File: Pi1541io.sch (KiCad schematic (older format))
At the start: 28 parts, among them J1 IEC1, J2 IEC2, J3 IEC3, J4 ExtSpkr, J5 GS3, J6 GS3, J7 GS3, J8 GS3, P1 Conn_02x20_Odd_Even, SW1 SW_Push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

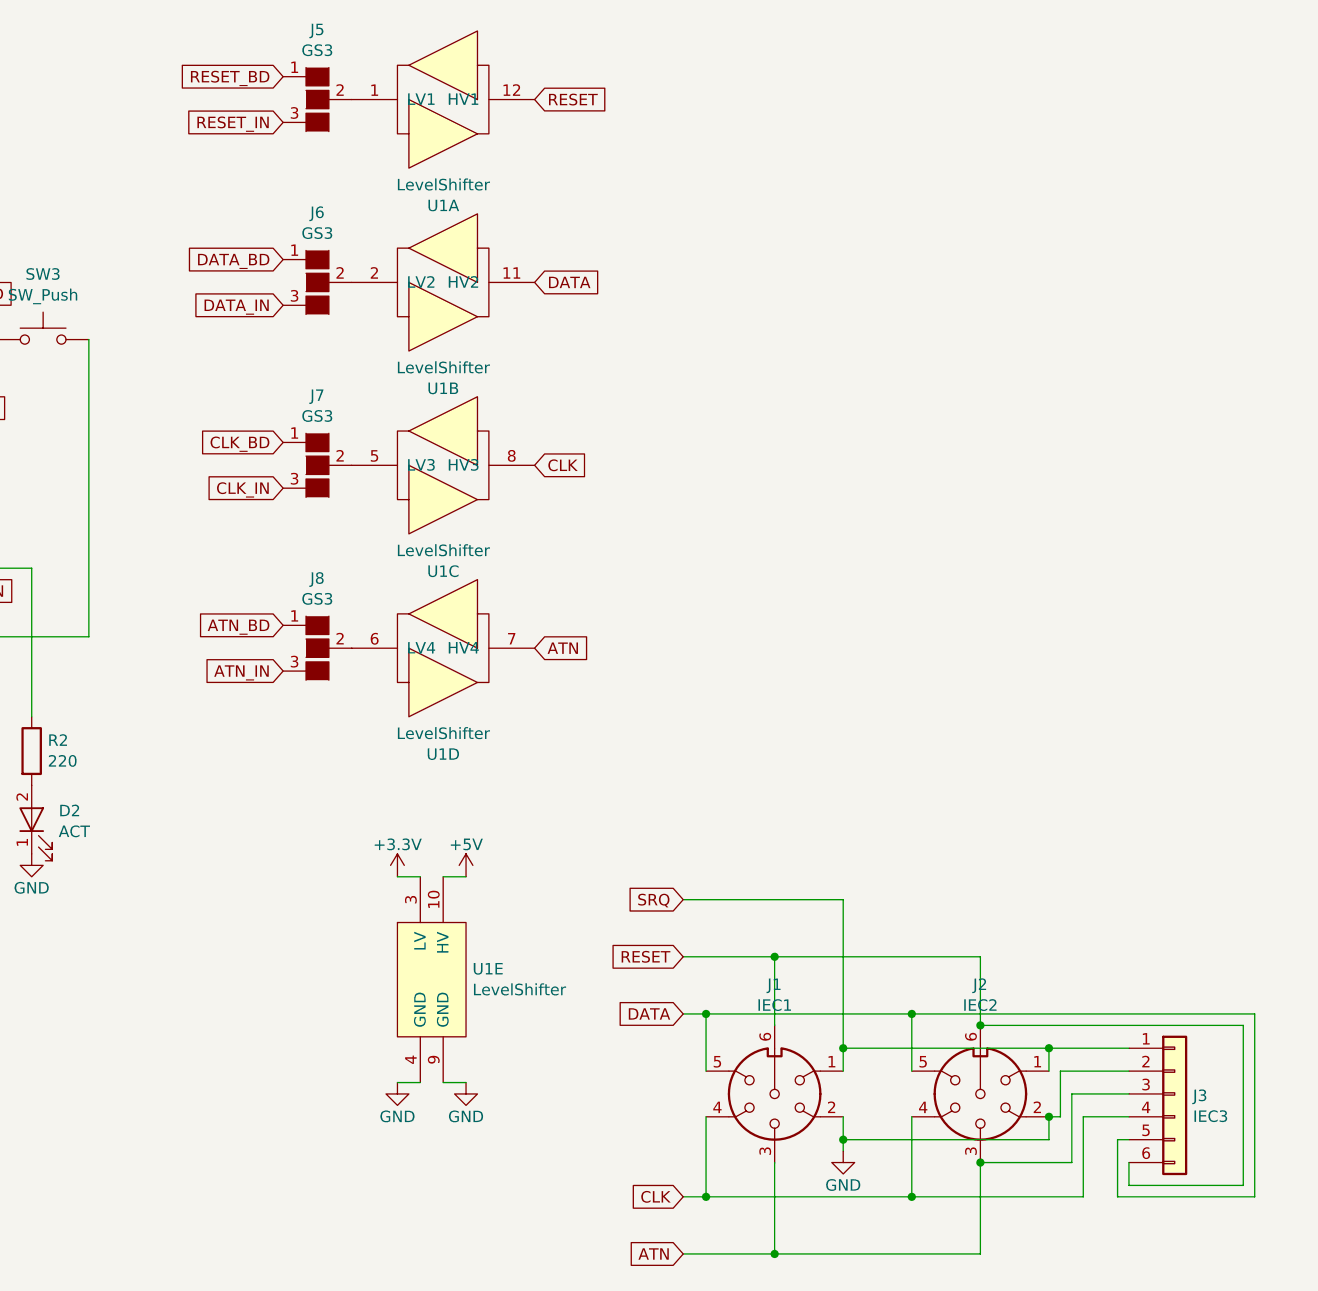
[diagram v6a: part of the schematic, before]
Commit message: Silk screen corrections. Re-added reset button.
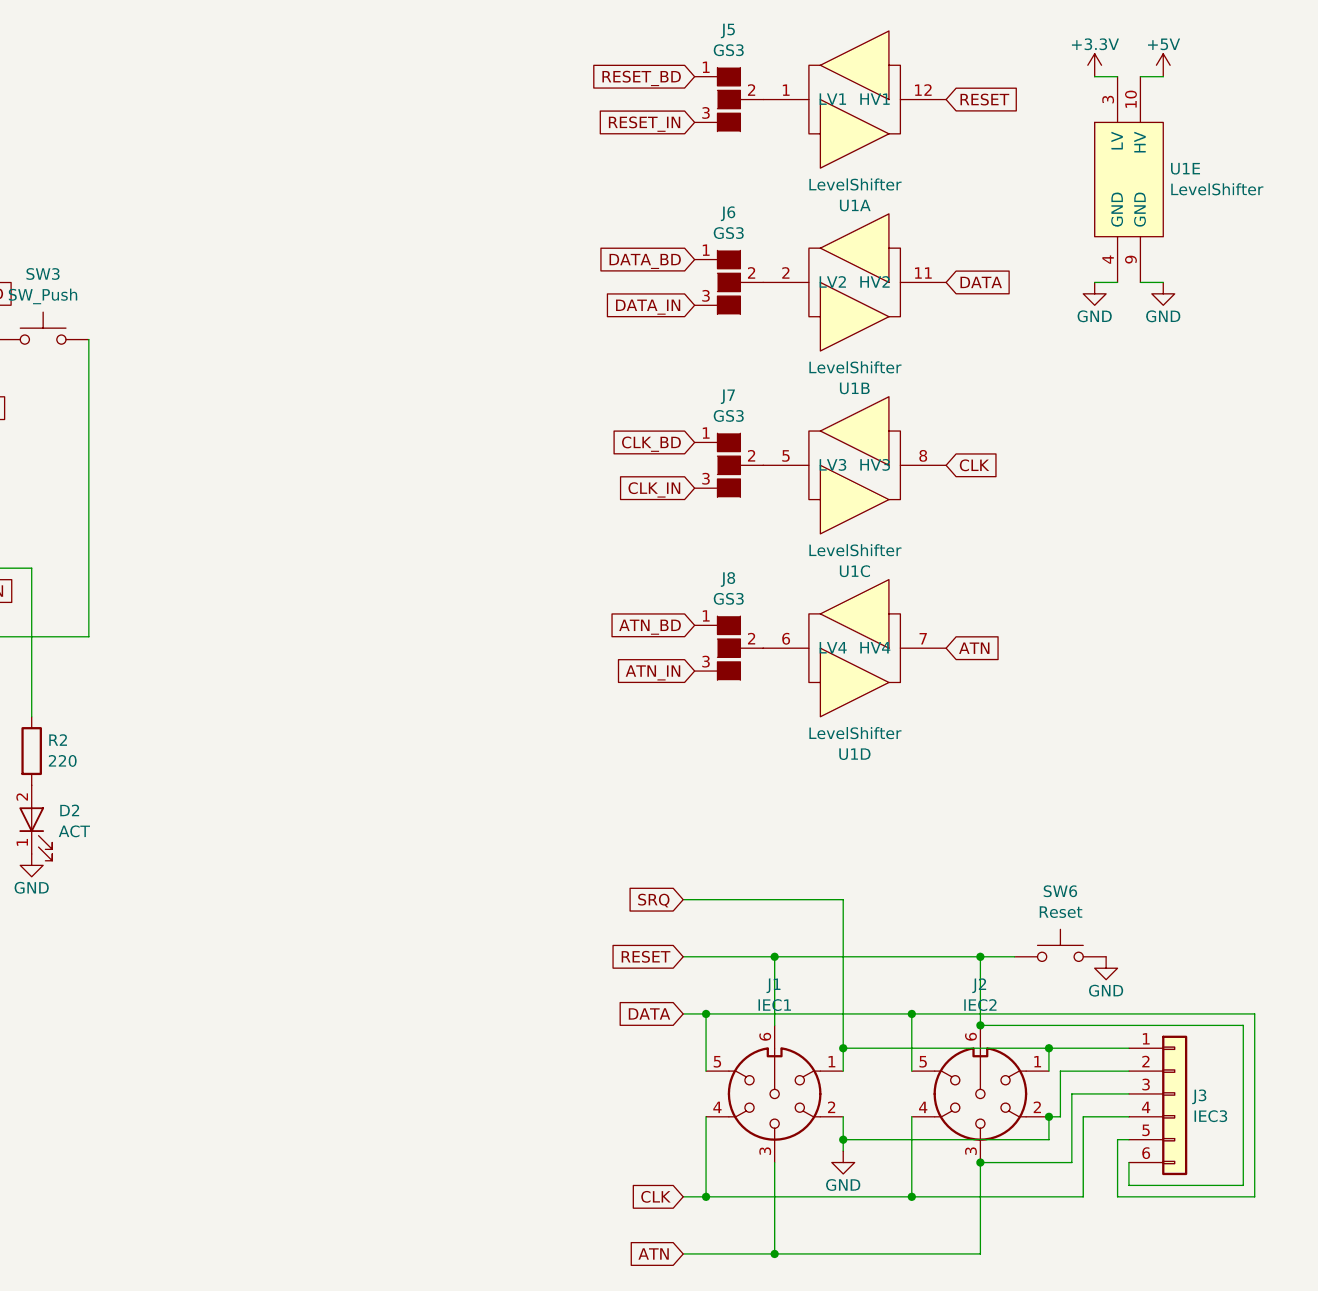
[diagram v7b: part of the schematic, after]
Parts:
- added SW6: Reset, Buttons_Switches_THT:SW_PUSH_6mm, symbol Switch:SW_Push
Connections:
- net GND: now also SW6.2
- net RESET: now also SW6.1
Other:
- moved on the sheet: J5, J6, J7, J8, U1A, U1B, U1C, U1D, U1E
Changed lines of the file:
@@
 Sheet 1 1
 Title "PI1541 IO Adapter"
-Date "2018-05-09"
-Rev "1"
+Date "2018-05-24"
+Rev "x"
 Comp "hackup.net"
 Comment1 "https://github.com/hackup/Pi1541io"
@@
 L hackup:LevelShifterModule4CH U1
 U 1 1 5AF39D90
-P 7350 1050
-F 0 "U1" H 7350 585 50  0000 C CNN
-F 1 "LevelShifter" H 7350 676 50  0000 C CNN
-F 2 "hackup:LevelShifterModule4CH" H 7350 1050 50  0001 C CNN
-F 3 "" H 7350 1050 50  0001 C CNN
-	1    7350 1050
+P 9150 1050
+F 0 "U1" H 9150 585 50  0000 C CNN
+F 1 "LevelShifter" H 9150 676 50  0000 C CNN
+F 2 "hackup:LevelShifterModule4CH" H 9150 1050 50  0001 C CNN
+F 3 "" H 9150 1050 50  0001 C CNN
+	1    9150 1050
 	1    0    0    -1
 $EndComp
@@
 L hackup:LevelShifterModule4CH U1
 U 5 1 5AF39E92
-P 7300 4900
-F 0 "U1" H 7478 4946 50  0000 L CNN
-F 1 "LevelShifter" H 7478 4855 50  0000 L CNN
-F 2 "hackup:LevelShifterModule4CH" H 7300 4900 50  0001 C CNN
-F 3 "" H 7300 4900 50  0001 C CNN
-	5    7300 4900
+P 10350 1400
+F 0 "U1" H 10528 1446 50  0000 L CNN
+F 1 "LevelShifter" H 10528 1355 50  0000 L CNN
+F 2 "hackup:LevelShifterModule4CH" H 10350 1400 50  0001 C CNN
+F 3 "" H 10350 1400 50  0001 C CNN
+	5    10350 1400
 	1    0    0    -1
 $EndComp
@@
 L hackup:LevelShifterModule4CH U1
 U 3 1 5AF3A14B
-P 7350 2650
-F 0 "U1" H 7350 2185 50  0000 C CNN
-F 1 "LevelShifter" H 7350 2276 50  0000 C CNN
-F 2 "hackup:LevelShifterModule4CH" H 7350 2650 50  0001 C CNN
-F 3 "" H 7350 2650 50  0001 C CNN
-	3    7350 2650
+P 9150 2650
+F 0 "U1" H 9150 2185 50  0000 C CNN
+F 1 "LevelShifter" H 9150 2276 50  0000 C CNN
+F 2 "hackup:LevelShifterModule4CH" H 9150 2650 50  0001 C CNN
+F 3 "" H 9150 2650 50  0001 C CNN
+	3    9150 2650
 	1    0    0    -1
 $EndComp
@@
 L hackup:LevelShifterModule4CH U1
 U 4 1 5AF3A181
-P 7350 3450
-F 0 "U1" H 7350 2985 50  0000 C CNN
-F 1 "LevelShifter" H 7350 3076 50  0000 C CNN
-F 2 "hackup:LevelShifterModule4CH" H 7350 3450 50  0001 C CNN
-F 3 "" H 7350 3450 50  0001 C CNN
-	4    7350 3450
+P 9150 3450
+F 0 "U1" H 9150 2985 50  0000 C CNN
+F 1 "LevelShifter" H 9150 3076 50  0000 C CNN
+F 2 "hackup:LevelShifterModule4CH" H 9150 3450 50  0001 C CNN
+F 3 "" H 9150 3450 50  0001 C CNN
+	4    9150 3450
 	1    0    0    -1
 $EndComp
@@
 L power:+5V #PWR0101
 U 1 1 5AF3A4FD
-P 7450 4450
-F 0 "#PWR0101" H 7450 4300 50  0001 C CNN
-F 1 "+5V" H 7450 4590 50  0000 C CNN
-F 2 "" H 7450 4450 50  0000 C CNN
-F 3 "" H 7450 4450 50  0000 C CNN
-	1    7450 4450
+P 10500 950
+F 0 "#PWR0101" H 10500 800 50  0001 C CNN
+F 1 "+5V" H 10500 1090 50  0000 C CNN
+F 2 "" H 10500 950 50  0000 C CNN
+F 3 "" H 10500 950 50  0000 C CNN
+	1    10500 950
 	1    0    0    -1
 $EndComp
@@
 L power:+3.3V #PWR0102
 U 1 1 5AF3A558
-P 7150 4450
-F 0 "#PWR0102" H 7150 4300 50  0001 C CNN
-F 1 "+3.3V" H 7150 4590 50  0000 C CNN
-F 2 "" H 7150 4450 50  0000 C CNN
-F 3 "" H 7150 4450 50  0000 C CNN
-	1    7150 4450
+P 10200 950
+F 0 "#PWR0102" H 10200 800 50  0001 C CNN
+F 1 "+3.3V" H 10200 1090 50  0000 C CNN
+F 2 "" H 10200 950 50  0000 C CNN
+F 3 "" H 10200 950 50  0000 C CNN
+	1    10200 950
 	1    0    0    -1
 $EndComp
@@
 L power:GND #PWR0103
 U 1 1 5AF3A635
-P 7150 5350
-F 0 "#PWR0103" H 7150 5100 50  0001 C CNN
-F 1 "GND" H 7150 5200 50  0000 C CNN
-F 2 "" H 7150 5350 50  0000 C CNN
-F 3 "" H 7150 5350 50  0000 C CNN
-	1    7150 5350
+P 10200 1850
+F 0 "#PWR0103" H 10200 1600 50  0001 C CNN
+F 1 "GND" H 10200 1700 50  0000 C CNN
+F 2 "" H 10200 1850 50  0000 C CNN
+F 3 "" H 10200 1850 50  0000 C CNN
+	1    10200 1850
 	1    0    0    -1
 $EndComp
@@
 L power:GND #PWR0104
 U 1 1 5AF3A654
-P 7450 5350
-F 0 "#PWR0104" H 7450 5100 50  0001 C CNN
-F 1 "GND" H 7450 5200 50  0000 C CNN
-F 2 "" H 7450 5350 50  0000 C CNN
-F 3 "" H 7450 5350 50  0000 C CNN
-	1    7450 5350
-	1    0    0    -1
-$EndComp
-Wire Wire Line
-	7250 4450 7150 4450
-Wire Wire Line
-	7350 4450 7450 4450
-Wire Wire Line
-	7350 5350 7450 5350
-Wire Wire Line
-	7250 5350 7150 5350
+P 10500 1850
+F 0 "#PWR0104" H 10500 1600 50  0001 C CNN
+F 1 "GND" H 10500 1700 50  0000 C CNN
+F 2 "" H 10500 1850 50  0000 C CNN
+F 3 "" H 10500 1850 50  0000 C CNN
+	1    10500 1850
+	1    0    0    -1
+$EndComp
+Wire Wire Line
+	10300 950  10200 950
+Wire Wire Line
+	10400 950  10500 950
+Wire Wire Line
+	10400 1850 10500 1850
+Wire Wire Line
+	10300 1850 10200 1850
 Text Label 2400 1500 0    50   ~ 0
 GPIO2(SDA1)
@@
 L hackup:LevelShifterModule4CH U1
 U 2 1 5AF87C0F
-P 7350 1850
-F 0 "U1" H 7350 1385 50  0000 C CNN
-F 1 "LevelShifter" H 7350 1476 50  0000 C CNN
-F 2 "hackup:LevelShifterModule4CH" H 7350 1850 50  0001 C CNN
-F 3 "" H 7350 1850 50  0001 C CNN
-	2    7350 1850
+P 9150 1850
+F 0 "U1" H 9150 1385 50  0000 C CNN
+F 1 "LevelShifter" H 9150 1476 50  0000 C CNN
+F 2 "hackup:LevelShifterModule4CH" H 9150 1850 50  0001 C CNN
+F 3 "" H 9150 1850 50  0001 C CNN
+	2    9150 1850
 	1    0    0    -1
 $EndComp
@@
 Wire Wire Line
 	8800 6100 8400 6100
-Text GLabel 6650 950  0    50   Input ~ 0
+Text GLabel 8450 950  0    50   Input ~ 0
 RESET_BD
-Text GLabel 6650 1750 0    50   Input ~ 0
+Text GLabel 8450 1750 0    50   Input ~ 0
 DATA_BD
-Text GLabel 6650 2550 0    50   Input ~ 0
+Text GLabel 8450 2550 0    50   Input ~ 0
 CLK_BD
-Text GLabel 6650 3350 0    50   Input ~ 0
+Text GLabel 8450 3350 0    50   Input ~ 0
 ATN_BD
 Text GLabel 2400 1600 0    50   Input ~ 0
@@
 Text GLabel 8400 4550 0    50   Input ~ 0
 SRQ
-Text GLabel 7750 1050 2    50   Input ~ 0
+Text GLabel 9550 1050 2    50   Input ~ 0
 RESET
-Text GLabel 7750 1850 2    50   Input ~ 0
+Text GLabel 9550 1850 2    50   Input ~ 0
 DATA
-Text GLabel 7750 2650 2    50   Input ~ 0
+Text GLabel 9550 2650 2    50   Input ~ 0
 CLK
-Text GLabel 7750 3450 2    50   Input ~ 0
+Text GLabel 9550 3450 2    50   Input ~ 0
 ATN
 Text GLabel 2350 3100 0    50   Input ~ 0
@@
 L conn:GS3 J5
 U 1 1 5B06E6C4
-P 6800 1050
-F 0 "J5" H 6800 1355 50  0000 C CNN
-F 1 "GS3" H 6800 1264 50  0000 C CNN
-F 2 "Connectors:GS3" V 6888 976 50  0001 C CNN
-F 3 "" H 6800 1050 50  0001 C CNN
-	1    6800 1050
+P 8600 1050
+F 0 "J5" H 8600 1355 50  0000 C CNN
+F 1 "GS3" H 8600 1264 50  0000 C CNN
+F 2 "Connectors:GS3" V 8688 976 50  0001 C CNN
+F 3 "" H 8600 1050 50  0001 C CNN
+	1    8600 1050
 	1    0    0    -1
 $EndComp
@@
 L conn:GS3 J6
 U 1 1 5B072B62
-P 6800 1850
-F 0 "J6" H 6800 2155 50  0000 C CNN
-F 1 "GS3" H 6800 2064 50  0000 C CNN
-F 2 "Connectors:GS3" V 6888 1776 50  0001 C CNN
-F 3 "" H 6800 1850 50  0001 C CNN
-	1    6800 1850
+P 8600 1850
+F 0 "J6" H 8600 2155 50  0000 C CNN
+F 1 "GS3" H 8600 2064 50  0000 C CNN
+F 2 "Connectors:GS3" V 8688 1776 50  0001 C CNN
+F 3 "" H 8600 1850 50  0001 C CNN
+	1    8600 1850
 	1    0    0    -1
 $EndComp
@@
 L conn:GS3 J7
 U 1 1 5B072BE3
-P 6800 2650
-F 0 "J7" H 6800 2955 50  0000 C CNN
-F 1 "GS3" H 6800 2864 50  0000 C CNN
-F 2 "Connectors:GS3" V 6888 2576 50  0001 C CNN
-F 3 "" H 6800 2650 50  0001 C CNN
-	1    6800 2650
+P 8600 2650
+F 0 "J7" H 8600 2955 50  0000 C CNN
+F 1 "GS3" H 8600 2864 50  0000 C CNN
+F 2 "Connectors:GS3" V 8688 2576 50  0001 C CNN
+F 3 "" H 8600 2650 50  0001 C CNN
+	1    8600 2650
 	1    0    0    -1
 $EndComp
@@
 L conn:GS3 J8
 U 1 1 5B072C85
-P 6800 3450
-F 0 "J8" H 6800 3755 50  0000 C CNN
-F 1 "GS3" H 6800 3664 50  0000 C CNN
-F 2 "Connectors:GS3" V 6888 3376 50  0001 C CNN
-F 3 "" H 6800 3450 50  0001 C CNN
-	1    6800 3450
-	1    0    0    -1
-$EndComp
-Text GLabel 6650 1150 0    50   Input ~ 0
+P 8600 3450
+F 0 "J8" H 8600 3755 50  0000 C CNN
+F 1 "GS3" H 8600 3664 50  0000 C CNN
+F 2 "Connectors:GS3" V 8688 3376 50  0001 C CNN
+F 3 "" H 8600 3450 50  0001 C CNN
+	1    8600 3450
+	1    0    0    -1
+$EndComp
+Text GLabel 8450 1150 0    50   Input ~ 0
 RESET_IN
-Text GLabel 6650 1950 0    50   Input ~ 0
+Text GLabel 8450 1950 0    50   Input ~ 0
 DATA_IN
-Text GLabel 6650 2750 0    50   Input ~ 0
+Text GLabel 8450 2750 0    50   Input ~ 0
 CLK_IN
-Text GLabel 6650 3550 0    50   Input ~ 0
+Text GLabel 8450 3550 0    50   Input ~ 0
 ATN_IN
 Text GLabel 5050 3200 2    50   Input ~ 0
@@
 Wire Wire Line
 	4000 4600 4000 4750
+$Comp
+L Switch:SW_Push SW6
+U 1 1 5B08095A
+P 10050 4800
+F 0 "SW6" H 10050 5085 50  0000 C CNN
+F 1 "Reset" H 10050 4994 50  0000 C CNN
+F 2 "Buttons_Switches_THT:SW_PUSH_6mm" H 10050 5000 50  0001 C CNN
+F 3 "" H 10050 5000 50  0001 C CNN
+	1    10050 4800
+	1    0    0    -1
+$EndComp
+$Comp
+L power:GND #PWR0109
+U 1 1 5B080A8A
+P 10250 4800
+F 0 "#PWR0109" H 10250 4550 50  0001 C CNN
+F 1 "GND" H 10250 4650 50  0000 C CNN
+F 2 "" H 10250 4800 50  0000 C CNN
+F 3 "" H 10250 4800 50  0000 C CNN
+	1    10250 4800
+	1    0    0    -1
+$EndComp
+Wire Wire Line
+	9850 4800 9700 4800
+Connection ~ 9700 4800
 $EndSCHEMATC

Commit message: Discrete components to optionally replace the level shifter module.
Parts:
- added Q1, Q2, Q3, Q4: BSS138, TO_SOT_Packages_SMD:SOT-23, symbol Transistor:BSS138
- added R10, R11, R12, R5, R6, R7, R8, R9: R, Resistors_SMD:R_0805, symbol device:R
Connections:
- net labels added: ATN_3V, CLK_3V, DATA_3V, RESET_3V
- wire segments 133 -> 149
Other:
- note added: "4 Channel Level Shifter Module"
- note added: "7406 Bus Driver (optional)"
- note added: "Discrete Level Shifter Components"
- note added: "Fit either a compatible level shifter module OR the discrete components!"
- moved on the sheet: C1, J5, J6, J7, J8, R3, R4, U1A, U1B, U1C, U1D, U1E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
